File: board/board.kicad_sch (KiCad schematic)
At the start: 96 parts, among them IC1 tps610981dser, IC2 LTR-303ALS-01, IC3 EFM32TG108F32-D-QFN24, IC4 AT30TS74-SS8M-B, IC5 ADA4528-2, IC6 TLV70245_SOT23-5, J1 Conn_01x05_Male, J2 , J3 , J4 , Q1 Q_PMOS_GSD, Q2 Q_PMOS_GSD

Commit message: Add MAN
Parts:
- BT1: MAN (none) -> Keystone; MPN KEYSTONE/3002 -> 3002
- C1, C10, C12, C16, C19, C2, C3, C4, C6: MAN (none) -> Murata Electronics
- C11, C13, C18, C5, C8: MAN (none) -> Samsung Electro-Mechanics
- C14, C17, C7, C9, MH1, MH2, MH3, MH4, MH5: MAN (none) -> Wurth Elektronik
- D1, D10, D11, D12, D13, D14, D15, D16, D17, D18, D19, D2, D20, D21, D22, D23, D24, D25, D26, D3, D4, D5, D6, D7, D8, D9: MAN (none) -> Inolux
- D28, D30, D31: MAN (none) -> Micro Commercial Co
- IC1: MAN (none) -> Texas Instruments
- IC2: MAN (none) -> Lite-On Inc
- IC3: MAN (none) -> Silicon Labs
- IC4: MAN (none) -> Microchip Technology
- IC5: MAN (none) -> Analog Devices
- IC6: DNF (none) -> OPTIONAL
- L1: MAN (none) -> TDK
- L2: MAN (none) -> Murata
- Q1, Q2: MAN (none) -> Vishay
- R1: DNF (none) -> OPTIONAL; MAN (none) -> Panasonic
- R10, R11, R16, R17, R18, R19, R2, R20, R21, R3, R4, R5, R6, R9: MAN (none) -> Panasonic
- R12, R7, R8: MAN (none) -> Stackpole Electronics Inc
- R13, R14, R15: MAN (none) -> Yageo

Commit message: add missing MAN fields
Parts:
- C15: MAN (none) -> Yageo
- IC6: MAN (none) -> Texas Instruments
- J1: MAN (none) -> Harwin Inc.
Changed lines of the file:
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@@
+      (effects (font (size 1.27 1.27)) hide)
+    )
+    (property "MAN" "Harwin Inc." (id 4) (at 254 69.85 0)
       (effects (font (size 1.27 1.27)) hide)
     )
@@
     )
     (property "DNF" "OPTIONAL" (id 5) (at 368.3 111.76 0)
+      (effects (font (size 1.27 1.27)) hide)
+    )
+    (property "MAN" "Yageo" (id 4) (at 368.3 111.76 0)
       (effects (font (size 1.27 1.27)) hide)
     )
@@
       (effects (font (size 1.27 1.27)) hide)
     )
+    (property "MAN" "Texas Instruments" (id 4) (at 383.54 52.07 0)
+      (effects (font (size 1.27 1.27)) hide)
+    )

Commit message: cheaper caps
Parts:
- C1, C10, C12, C16, C2, C3, C4, C6: MAN Murata Electronics -> Taiyo Yuden; MPN GRM188R60J106ME84D -> JMK107ABJ106MA-T
- IC3: MPN EFM32TG108F32-D-QFN24 -> EFM32TG108F32-QFN24
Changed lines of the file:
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@@
       (effects (font (size 1.27 1.27)) hide)
     )
-    (property "MPN" "GRM188R60J106ME84D" (id 4) (at 24.13 134.62 90)
-      (effects (font (size 1.27 1.27)) hide)
-    )
-    (property "MAN" "Murata Electronics" (id 5) (at 24.13 134.62 90)
+    (property "MPN" "JMK107ABJ106MA-T" (id 4) (at 24.13 134.62 90)
+      (effects (font (size 1.27 1.27)) hide)
+    )
+    (property "MAN" "Taiyo Yuden" (id 5) (at 24.13 134.62 90)
       (effects (font (size 1.27 1.27)) hide)
     )
@@
       (effects (font (size 1.27 1.27)) hide)
     )
-    (property "MPN" "GRM188R60J106ME84D" (id 4) (at 24.13 177.8 90)
-      (effects (font (size 1.27 1.27)) hide)
-    )
-    (property "MAN" "Murata Electronics" (id 5) (at 24.13 177.8 90)
+    (property "MPN" "JMK107ABJ106MA-T" (id 4) (at 24.13 177.8 90)
+      (effects (font (size 1.27 1.27)) hide)
+    )
+    (property "MAN" "Taiyo Yuden" (id 5) (at 24.13 177.8 90)
       (effects (font (size 1.27 1.27)) hide)
     )
@@
       (effects (font (size 1.27 1.27)) hide)
     )
-    (property "MPN" "GRM188R60J106ME84D" (id 4) (at 38.1 177.8 90)
-      (effects (font (size 1.27 1.27)) hide)
-    )
-    (property "MAN" "Murata Electronics" (id 5) (at 38.1 177.8 90)
+    (property "MPN" "JMK107ABJ106MA-T" (id 4) (at 38.1 177.8 90)
+      (effects (font (size 1.27 1.27)) hide)
+    )
+    (property "MAN" "Taiyo Yuden" (id 5) (at 38.1 177.8 90)
       (effects (font (size 1.27 1.27)) hide)
     )
@@
       (effects (font (size 1.27 1.27)) hide)
     )
-    (property "MPN" "GRM188R60J106ME84D" (id 4) (at 53.34 177.8 90)
-      (effects (font (size 1.27 1.27)) hide)
-    )
-    (property "MAN" "Murata Electronics" (id 5) (at 53.34 177.8 90)
+    (property "MPN" "JMK107ABJ106MA-T" (id 4) (at 53.34 177.8 90)
+      (effects (font (size 1.27 1.27)) hide)
+    )
+    (property "MAN" "Taiyo Yuden" (id 5) (at 53.34 177.8 90)
       (effects (font (size 1.27 1.27)) hide)
     )
@@
       (effects (font (size 1.27 1.27)) hide)
     )
-    (property "MPN" "GRM188R60J106ME84D" (id 4) (at 82.55 156.21 90)
-      (effects (font (size 1.27 1.27)) hide)
-    )
-    (property "MAN" "Murata Electronics" (id 5) (at 82.55 156.21 90)
+    (property "MPN" "JMK107ABJ106MA-T" (id 4) (at 82.55 156.21 90)
+      (effects (font (size 1.27 1.27)) hide)
+    )
+    (property "MAN" "Taiyo Yuden" (id 5) (at 82.55 156.21 90)
       (effects (font (size 1.27 1.27)) hide)
     )
@@
       (effects (font (size 1.27 1.27)) hide)
     )
-    (property "MPN" "GRM188R60J106ME84D" (id 4) (at 123.19 82.55 0)
-      (effects (font (size 1.27 1.27)) hide)
-    )
-    (property "MAN" "Murata Electronics" (id 5) (at 123.19 82.55 0)
+    (property "MPN" "JMK107ABJ106MA-T" (id 4) (at 123.19 82.55 0)
+      (effects (font (size 1.27 1.27)) hide)
+    )
+    (property "MAN" "Taiyo Yuden" (id 5) (at 123.19 82.55 0)
       (effects (font (size 1.27 1.27)) hide)
     )
@@
       (effects (font (size 1.27 1.27)) hide)
     )
-    (property "MPN" "GRM188R60J106ME84D" (id 4) (at 214.63 140.97 90)
-      (effects (font (size 1.27 1.27)) hide)
-    )
-    (property "MAN" "Murata Electronics" (id 5) (at 214.63 140.97 90)
+    (property "MPN" "JMK107ABJ106MA-T" (id 4) (at 214.63 140.97 90)
+      (effects (font (size 1.27 1.27)) hide)
+    )
+    (property "MAN" "Taiyo Yuden" (id 5) (at 214.63 140.97 90)
       (effects (font (size 1.27 1.27)) hide)
     )
@@
       (effects (font (size 1.27 1.27)) hide)
     )
-    (property "MPN" "GRM188R60J106ME84D" (id 4) (at 237.49 120.65 0)
-      (effects (font (size 1.27 1.27)) hide)
-    )
-    (property "MAN" "Murata Electronics" (id 5) (at 237.49 120.65 0)
+    (property "MPN" "JMK107ABJ106MA-T" (id 4) (at 237.49 120.65 0)
+      (effects (font (size 1.27 1.27)) hide)
+    )
+    (property "MAN" "Taiyo Yuden" (id 5) (at 237.49 120.65 0)
       (effects (font (size 1.27 1.27)) hide)
     )
@@
       (effects (font (size 1.27 1.27)) hide)
     )
-    (property "MPN" "EFM32TG108F32-D-QFN24 " (id 4) (at 190.5 101.6 0)
-      (effects (font (size 1.27 1.27)) hide)
-    )
+    (property "MPN" "EFM32TG108F32-QFN24" (id 4) (at 190.5 101.6 0)
+      (effects (font (size 1.27 1.27)) hide)
+    )

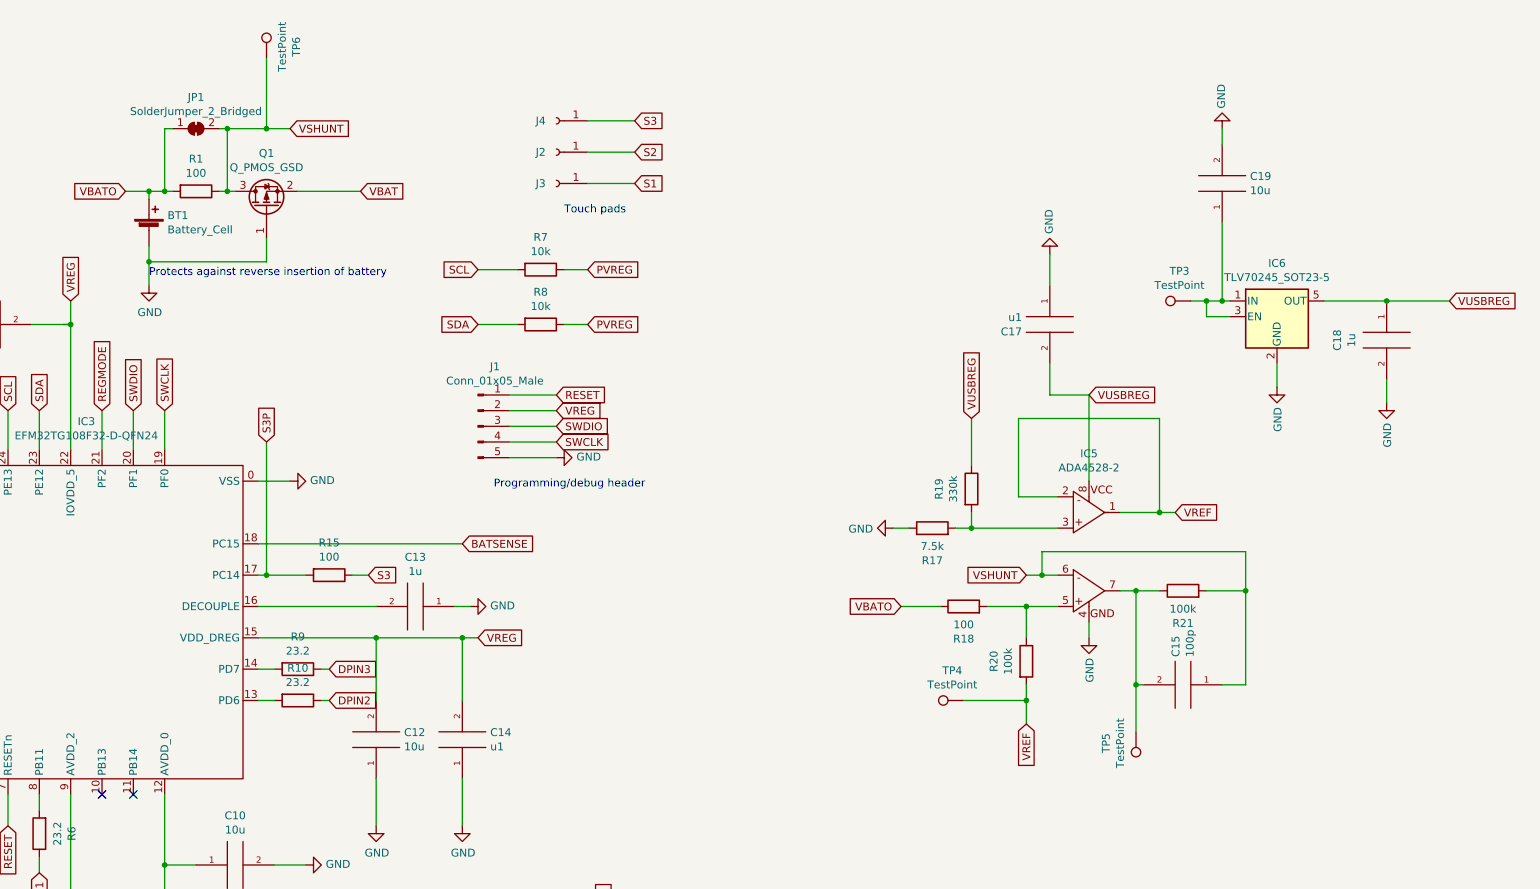
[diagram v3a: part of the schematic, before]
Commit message: remove microcurrent
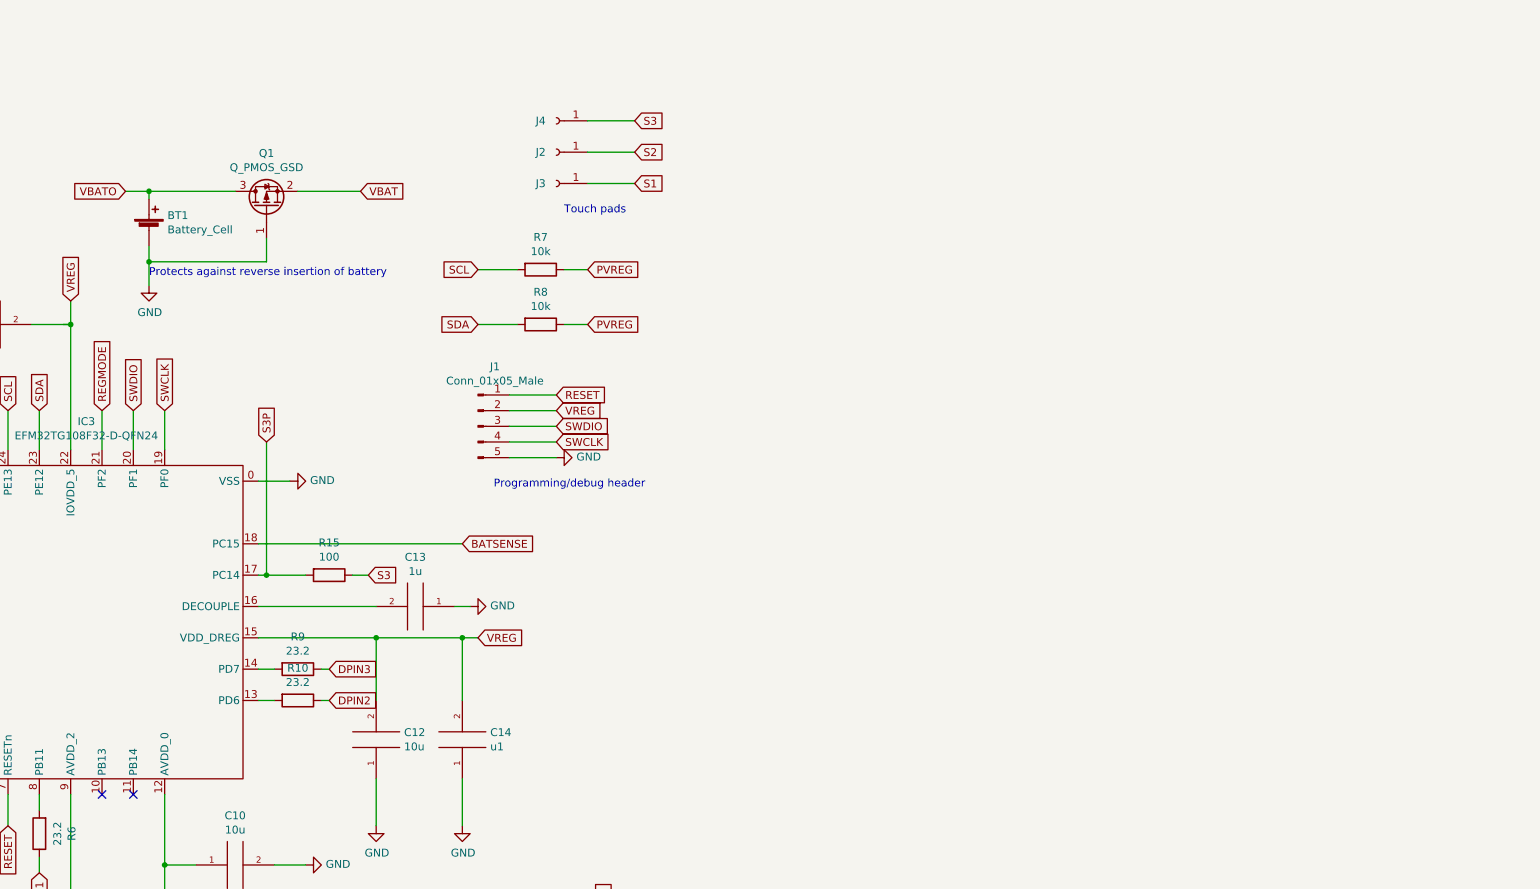
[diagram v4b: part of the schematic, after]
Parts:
- removed C15: 100p, mlm:0603, symbol pspice:CAP
- removed C17: u1, mlm:0603, symbol pspice:CAP
- removed C18: 1u, mlm:0603, symbol pspice:CAP
- removed C19: 10u, mlm:0603, symbol pspice:CAP
- removed IC5: ADA4528-2, mlm:ADA4528-2, symbol mlm:ADA4528-2
- removed IC6: TLV70245_SOT23-5, Package_TO_SOT_SMD:SOT-23-5, symbol Regulator_Linear:TLV70245_SOT23-5
- removed JP1: SolderJumper_2_Bridged, Jumper:SolderJumper-2_P1.3mm_Open_Pad1.0x1.5mm, symbol Jumper:SolderJumper_2_Bridged
- removed R1, R18: 100, mlm:0603, symbol Device:R
- removed R17: 7.5k, mlm:0603, symbol Device:R
- removed R19: 330k, mlm:0603, symbol Device:R
- removed R20, R21: 100k, mlm:0603, symbol Device:R
- removed TP3, TP6: TestPoint, TestPoint:TestPoint_Pad_3.0x3.0mm, symbol Connector:TestPoint
- removed TP4, TP5: TestPoint, TestPoint:TestPoint_Pad_D1.5mm, symbol Connector:TestPoint
- J1: MPN M20-7910542R -> (none)
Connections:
- net VSHUNT is gone; now on net VBATO: Q1.3 (D)

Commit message: zone fill issues
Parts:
- added C15: 10u, mlm:0603, symbol pspice:CAP
- added C17, C18: u1, mlm:0603, symbol pspice:CAP
- C1: value 10u -> 4u7; footprint mlm:0603 -> Capacitor_SMD:C_1206_3216Metric; MAN Taiyo Yuden -> Kemet; MPN JMK107ABJ106MA-T -> C1206C475J3RACTU
- L1: value 4u7 -> 2u2; MAN TDK -> Taiyo Yuden; MPN VLS3015CX-4R7M-1 -> NRS4010T2R2MDGG
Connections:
- net GND: now also C15.1, C17.1, C18.2
- net VBAT: now also C15.2, C17.2, C18.1
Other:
- moved on the sheet: C16, C2, C3, L1

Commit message: remove temp sensor
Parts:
- removed IC4: AT30TS74-SS8M-B, Package_SO:SOIC-8_3.9x4.9mm_P1.27mm, symbol mlm:AT30TS74-SS8M-B
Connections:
- no-connect marks 9 -> 8
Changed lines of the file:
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@@
   (junction (at 86.36 63.5) (diameter 1.016) (color 0 0 0 0))
   (junction (at 86.36 76.2) (diameter 1.016) (color 0 0 0 0))
-  (junction (at 93.98 119.38) (diameter 1.016) (color 0 0 0 0))
-  (junction (at 93.98 123.19) (diameter 1.016) (color 0 0 0 0))
   (junction (at 95.25 25.4) (diameter 1.016) (color 0 0 0 0))
   (junction (at 95.25 66.04) (diameter 1.016) (color 0 0 0 0))
@@
   (junction (at 237.49 104.14) (diameter 1.016) (color 0 0 0 0))
   (junction (at 251.46 104.14) (diameter 1.016) (color 0 0 0 0))
-  (no_connect (at 27.94 217.17))
-  (no_connect (at 72.39 119.38))
-  (no_connect (at 27.94 227.33))
-  (no_connect (at 198.12 129.54))
   (no_connect (at 193.04 129.54))
-  (no_connect (at 138.43 158.75))
-  (no_connect (at 35.56 234.95))
+  (no_connect (at 198.12 129.54))
   (no_connect (at 41.91 227.33))
   (no_connect (at 41.91 217.17))
+  (no_connect (at 27.94 217.17))
+  (no_connect (at 35.56 234.95))
+  (no_connect (at 138.43 158.75))
+  (no_connect (at 27.94 227.33))
   (wire (pts (xy 3.81 167.64) (xy 6.35 167.64))
     (stroke (width 0) (type solid) (color 0 0 0 0))
@@
     (stroke (width 0) (type solid) (color 0 0 0 0))
   )
-  (wire (pts (xy 72.39 111.76) (xy 67.31 111.76))
-    (stroke (width 0) (type solid) (color 0 0 0 0))
-  )
-  (wire (pts (xy 72.39 115.57) (xy 67.31 115.57))
-    (stroke (width 0) (type solid) (color 0 0 0 0))
-  )
-  (wire (pts (xy 72.39 123.19) (xy 67.31 123.19))
-    (stroke (width 0) (type solid) (color 0 0 0 0))
-  )
   (wire (pts (xy 73.66 12.7) (xy 73.66 15.24))
     (stroke (width 0) (type solid) (color 0 0 0 0))
@@
     (stroke (width 0) (type solid) (color 0 0 0 0))
   )
-  (wire (pts (xy 90.17 111.76) (xy 93.98 111.76))
-    (stroke (width 0) (type solid) (color 0 0 0 0))
-  )
-  (wire (pts (xy 90.17 115.57) (xy 93.98 115.57))
-    (stroke (width 0) (type solid) (color 0 0 0 0))
-  )
   (wire (pts (xy 92.71 176.53) (xy 90.17 176.53))
     (stroke (width 0) (type solid) (color 0 0 0 0))
   )
-  (wire (pts (xy 93.98 115.57) (xy 93.98 119.38))
-    (stroke (width 0) (type solid) (color 0 0 0 0))
-  )
-  (wire (pts (xy 93.98 119.38) (xy 90.17 119.38))
-    (stroke (width 0) (type solid) (color 0 0 0 0))
-  )
-  (wire (pts (xy 93.98 119.38) (xy 93.98 123.19))
-    (stroke (width 0) (type solid) (color 0 0 0 0))
-  )
-  (wire (pts (xy 93.98 123.19) (xy 90.17 123.19))
-    (stroke (width 0) (type solid) (color 0 0 0 0))
-  )
-  (wire (pts (xy 93.98 123.19) (xy 93.98 127))
-    (stroke (width 0) (type solid) (color 0 0 0 0))
-  )
   (wire (pts (xy 95.25 12.7) (xy 95.25 25.4))
     (stroke (width 0) (type solid) (color 0 0 0 0))
@@
     (effects (font (size 1.27 1.27)) (justify right))
   )
-  (global_label "SDA" (shape input) (at 67.31 111.76 180)
-    (effects (font (size 1.27 1.27)) (justify right))
-  )
-  (global_label "SCL" (shape input) (at 67.31 115.57 180)
-    (effects (font (size 1.27 1.27)) (justify right))
-  )
   (global_label "REGMODE" (shape input) (at 78.74 182.88 270)
     (effects (font (size 1.27 1.27)) (justify right))
@@
     (effects (font (size 1.27 1.27)) (justify left))
   )
-  (global_label "PVREG" (shape input) (at 93.98 111.76 0)
-    (effects (font (size 1.27 1.27)) (justify left))
-  )
   (global_label "S1P" (shape input) (at 101.6 184.15 270)
     (effects (font (size 1.27 1.27)) (justify right))
@@
     )
   )
-  (symbol (lib_id "power:GND") (at 67.31 123.19 270) (unit 1)
-    (in_bom yes) (on_board yes)
-    (property "Reference" "#PWR0103" (id 0) (at 60.96 123.19 0)
-      (effects (font (size 1.27 1.27)) hide)
-    )
-    (property "Value" "GND" (id 1) (at 62.9158 123.317 0))
-    (property "Footprint" "" (id 2) (at 67.31 123.19 0)
-      (effects (font (size 1.27 1.27)) hide)
-    )
-    (property "Datasheet" "" (id 3) (at 67.31 123.19 0)
-      (effects (font (size 1.27 1.27)) hide)
-    )
-  )
   (symbol (lib_id "power:GND") (at 68.58 143.51 90) (unit 1)
     (in_bom yes) (on_board yes)
@@
     )
   )
-  (symbol (lib_id "power:GND") (at 93.98 127 0) (unit 1)
-    (in_bom yes) (on_board yes)
-    (property "Reference" "#PWR0101" (id 0) (at 93.98 133.35 0)
-      (effects (font (size 1.27 1.27)) hide)
-    )
-    (property "Value" "GND" (id 1) (at 94.107 131.3942 0))
-    (property "Footprint" "" (id 2) (at 93.98 127 0)
-      (effects (font (size 1.27 1.27)) hide)
-    )
-    (property "Datasheet" "" (id 3) (at 93.98 127 0)
-      (effects (font (size 1.27 1.27)) hide)
-    )
-  )
   (symbol (lib_id "power:GND") (at 114.3 156.21 270) (unit 1)
     (in_bom yes) (on_board yes)
@@
     )
   )
-  (symbol (lib_id "mlm:AT30TS74-SS8M-B") (at 81.28 116.84 0) (unit 1)
-    (in_bom yes) (on_board yes)
-    (property "Reference" "IC4" (id 0) (at 81.28 106.045 0))
-    (property "Value" "AT30TS74-SS8M-B" (id 1) (at 81.28 108.3564 0))
-    (property "Footprint" "Package_SO:SOIC-8_3.9x4.9mm_P1.27mm" (id 2) (at 76.2 114.3 0)
-      (effects (font (size 1.27 1.27)) hide)
-    )
-    (property "Datasheet" "" (id 3) (at 76.2 114.3 0)
-      (effects (font (size 1.27 1.27)) hide)
-    )
-    (property "MPN" "AT30TS74-SS8M-B" (id 4) (at 81.28 116.84 0)
-      (effects (font (size 1.27 1.27)) hide)
-    )
-    (property "MAN" "Microchip Technology" (id 5) (at 81.28 116.84 0)
-      (effects (font (size 1.27 1.27)) hide)
-    )
-  )
   (symbol (lib_id "mlm:tps610986") (at 52.07 148.59 0) (unit 1)
     (in_bom yes) (on_board yes)
@@
       (reference "#PWR021") (unit 1) (value "GND") (footprint "")
     )
-    (path "/9f05b4bc-24a0-4f3c-b3e3-ccf1739d8d75"
-      (reference "#PWR0101") (unit 1) (value "GND") (footprint "")
-    )
     (path "/a04503d3-704e-464c-8cc1-3a97192a7e30"
       (reference "#PWR0102") (unit 1) (value "GND") (footprint "")
     )
-    (path "/41d34b82-4f14-4504-9eb1-0c1ae10dd9c0"
-      (reference "#PWR0103") (unit 1) (value "GND") (footprint "")
-    )
     (path "/85767743-1d7f-4c58-8b35-4ff1e495c454"
       (reference "#PWR0104") (unit 1) (value "GND") (footprint "")
@@
       (reference "IC3") (unit 1) (value "EFM32TG108F32-D-QFN24 ") (footprint "mlm:EFM32TG108_QFN24")
     )
-    (path "/10b29009-6008-4647-ac93-85ba9557f396"
-      (reference "IC4") (unit 1) (value "AT30TS74-SS8M-B") (footprint "Package_SO:SOIC-8_3.9x4.9mm_P1.27mm")
-    )
     (path "/90309286-8c4d-41f8-89bb-39ea2c179072"

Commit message: use new inductor footprint
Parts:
- L1: footprint mlm:VLS3015CX-4R7M-1 -> mlm:NRS4010T2R2MDGG
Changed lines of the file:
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@@
     (property "Reference" "L1" (id 0) (at 24.13 157.099 0))
     (property "Value" "2u2" (id 1) (at 17.78 156.87 0))
-    (property "Footprint" "mlm:VLS3015CX-4R7M-1" (id 2) (at 17.78 154.94 0)
+    (property "Footprint" "mlm:NRS4010T2R2MDGG" (id 2) (at 17.78 154.94 0)
       (effects (font (size 1.27 1.27)) hide)
     )
@@
     )
     (path "/684a6a55-19df-41c4-8df7-ad8b5e1629e7"
-      (reference "L1") (unit 1) (value "2u2") (footprint "mlm:VLS3015CX-4R7M-1")
+      (reference "L1") (unit 1) (value "2u2") (footprint "mlm:NRS4010T2R2MDGG")
     )
     (path "/3777c052-8d7f-48be-8f35-be4b3f40b0ff"
